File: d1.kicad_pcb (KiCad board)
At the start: 2 copper layers, 393.7 x 228.6 mm, 172 parts, among them J1 Conn_01x06, J12 Y, J13 Conn_01x16, J2 Conn_01x04, J3 EDAC 305-044-520-201, J4 W, J5 X, J6 S, J7 R, J8 T, J9 Z, Q1 Q_NPN_EBC, Q2 Q_PNP_EBC, Q3 Q_NPN_EBC, Q4 Q_PNP_EBC, Q5 MPS3704, Y1 14.31818 MHz

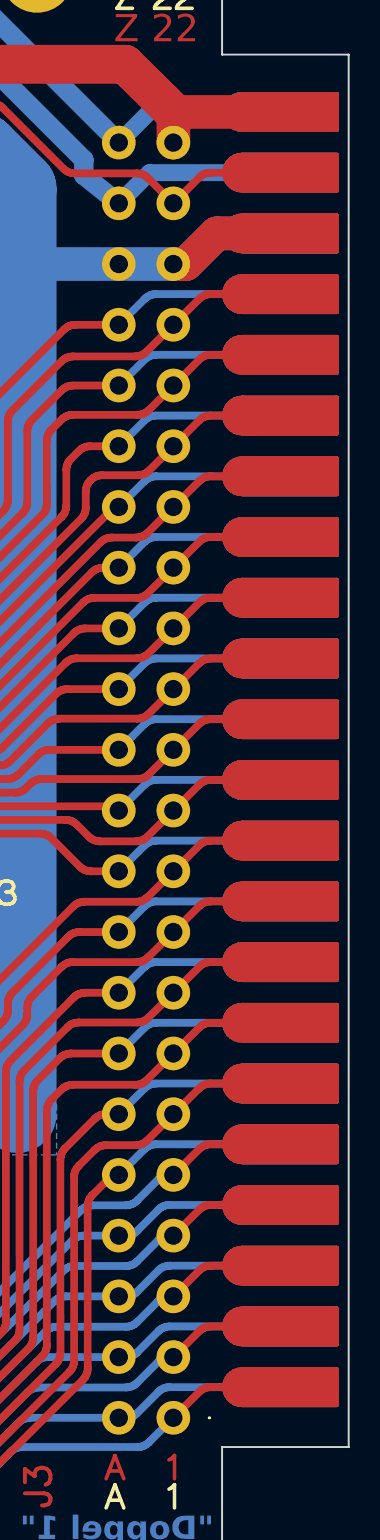
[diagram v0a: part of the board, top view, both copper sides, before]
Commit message: Created edge finger footprint
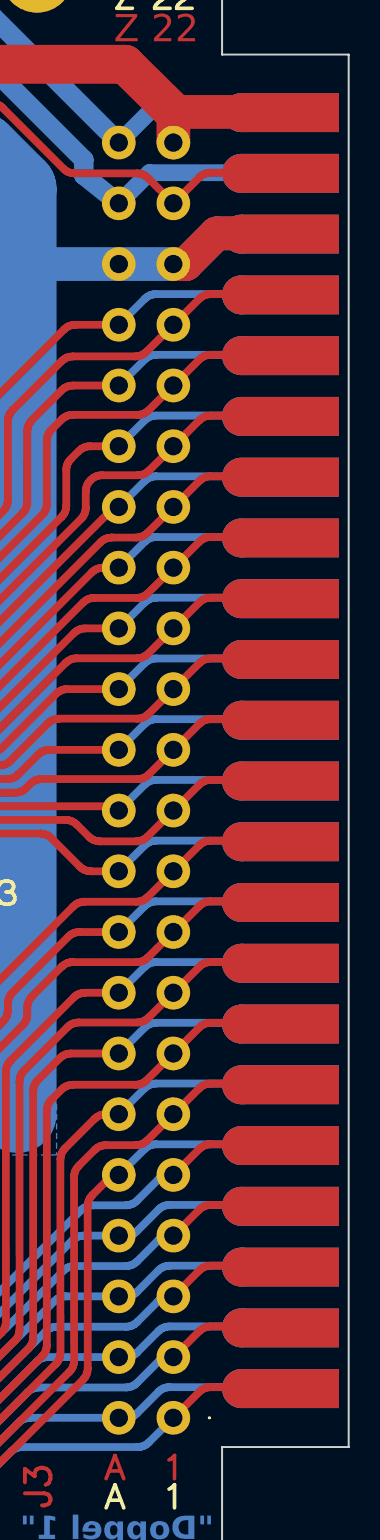
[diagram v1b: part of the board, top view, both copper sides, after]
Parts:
- added REF**: A1EdgeFingers, mainboard:A1EdgeFingers, F.Cu at (455.3, 310.5)
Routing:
- net GND: track 3263.4 -> 2945.1 mm
- net /Processor Section/ɸ2: track 876.4 -> 714.5 mm
- net -12V_UNREG: track 311.9 -> 152.1 mm
- net +5V: track 2653.9 -> 2494.7 mm
- net /Processor Section/A3: track 604.8 -> 445.7 mm
- net Net-(J7-~): track 381.6 -> 222.5 mm
- net /Processor Section/ɸ1: track 846.6 -> 687.5 mm
- net /Processor Section/~{NMI}: track 446.6 -> 287.5 mm
- net /Processor Section/~{IRQ}: track 434.4 -> 275.2 mm
- net /Processor Section/RDY: track 427.9 -> 268.8 mm
- net /Processor Section/D7: track 688.8 -> 529.7 mm
- net /Processor Section/D5: track 675.9 -> 516.8 mm
- net /Processor Section/A1: track 688.5 -> 529.4 mm
- net +12V_UNREG: track 314.9 -> 155.8 mm
- net /Processor Section/~{RES}: track 560.9 -> 401.8 mm
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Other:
- outline, holes or cut-outs redrawn
